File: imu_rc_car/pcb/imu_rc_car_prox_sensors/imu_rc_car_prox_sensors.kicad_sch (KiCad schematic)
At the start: 15 parts, among them J1 Conn_01x03_Socket, U1 LMV358

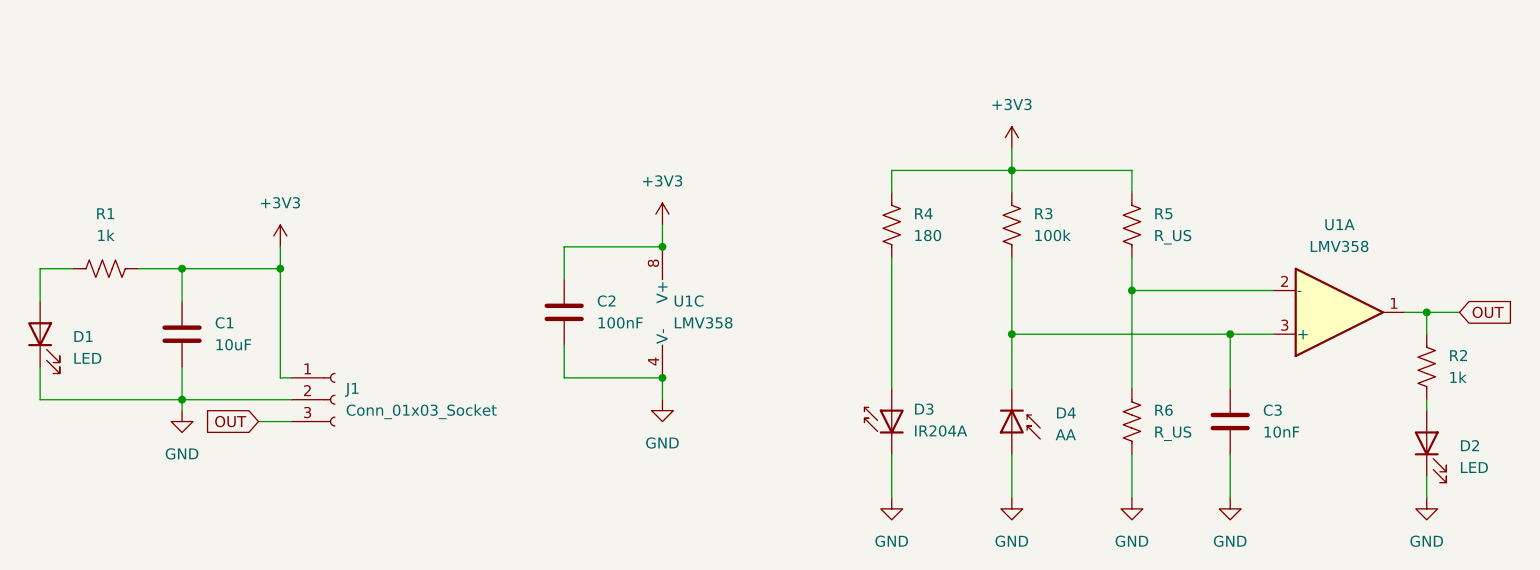
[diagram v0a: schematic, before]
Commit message: commit #23
minor changes to chassis 3d file
added proximity sensor 3d casing
v1.1.0 prox sensor board, featuring a band-pass filter and clk input
minor formatting to the src code
added function to update RSSI bars
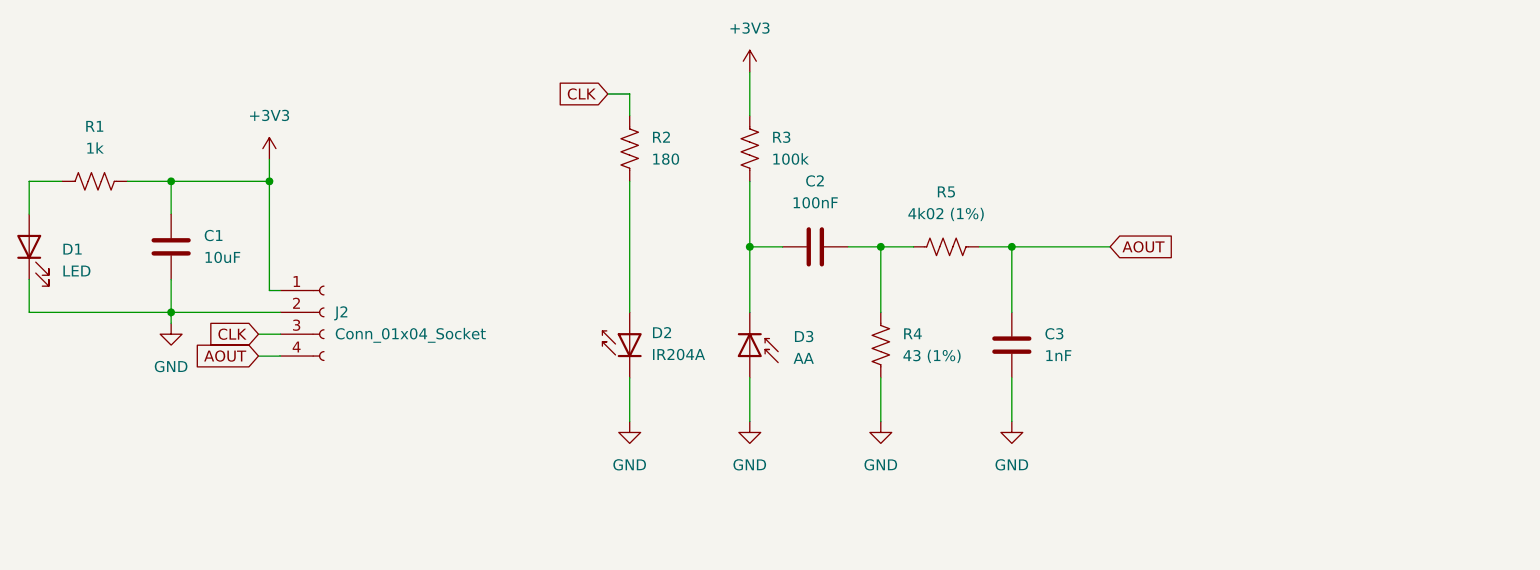
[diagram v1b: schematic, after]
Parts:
- removed D2: LED, LED_SMD:LED_0805_2012Metric, symbol Device:LED
- removed J1: Conn_01x03_Socket, Connector_JST:JST_PH_S3B-PH-SM4-TB_1x03-1MP_P2.00mm_Horizontal, symbol Connector:Conn_01x03_Socket
- removed R2: 1k, Resistor_SMD:R_0805_2012Metric, symbol Device:R_US
- removed R6: R_US, Resistor_SMD:R_0805_2012Metric, symbol Device:R_US
- removed U1: LMV358, Package_SO:MSOP-8_3x3mm_P0.65mm, symbol Amplifier_Operational:LMV358
- added J2: Conn_01x04_Socket, IMURCLibrary:JST_PH_S4B-PH-SM4-TB_1x04-1MP_P2.00mm_Horizontal, symbol Connector:Conn_01x04_Socket
- added R4: 43 (1%), Resistor_SMD:R_0805_2012Metric, symbol Device:R_US
- C3: value 10nF -> 1nF
- D2: renamed from D3; footprint LED_THT:LED_D3.0mm_IRBlack -> LED_THT:LED_D5.0mm_Horizontal_O1.27mm_Z3.0mm_Clear
- D3: renamed from D4; footprint LED_THT:LED_D3.0mm_IRBlack -> LED_THT:LED_D5.0mm_Horizontal_O1.27mm_Z3.0mm_IRBlack
- R5: value R_US -> 4k02 (1%)
- renumbered R4 to R2
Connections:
- net +3V3: now also J2.1 (Pin_1); no longer C2.1, R2.2, R5.2
- net GND: now also C3.1, J2.2 (Pin_2), R4.1; no longer C2.2, C3.2
- net at D3.1 (K), R3.1: now also C2.1; no longer C3.1
- net AOUT: now reaches R5.1
- net AOUT: now also C3.2, J2.4 (Pin_4)
- new net: C2.2, R4.2, R5.2
- new net CLK: J2.3 (Pin_3), R2.2
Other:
- moved on the sheet: C1, D1, D2, D3, R1, R2, R3
